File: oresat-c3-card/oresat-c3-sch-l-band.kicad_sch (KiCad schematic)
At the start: 71 parts, among them U15 Qorvo 856930, U16 AT86RF215, U17 SI4112-GM, U2 BP0805A1308, U23 NCS2-62+, U3 BP0805A1308, U4 BGB741L7ESD, U41 TQP3M9036, U5 BP0805A1308, U7 MAC-24+, X1 TXETALSANF-26.000000

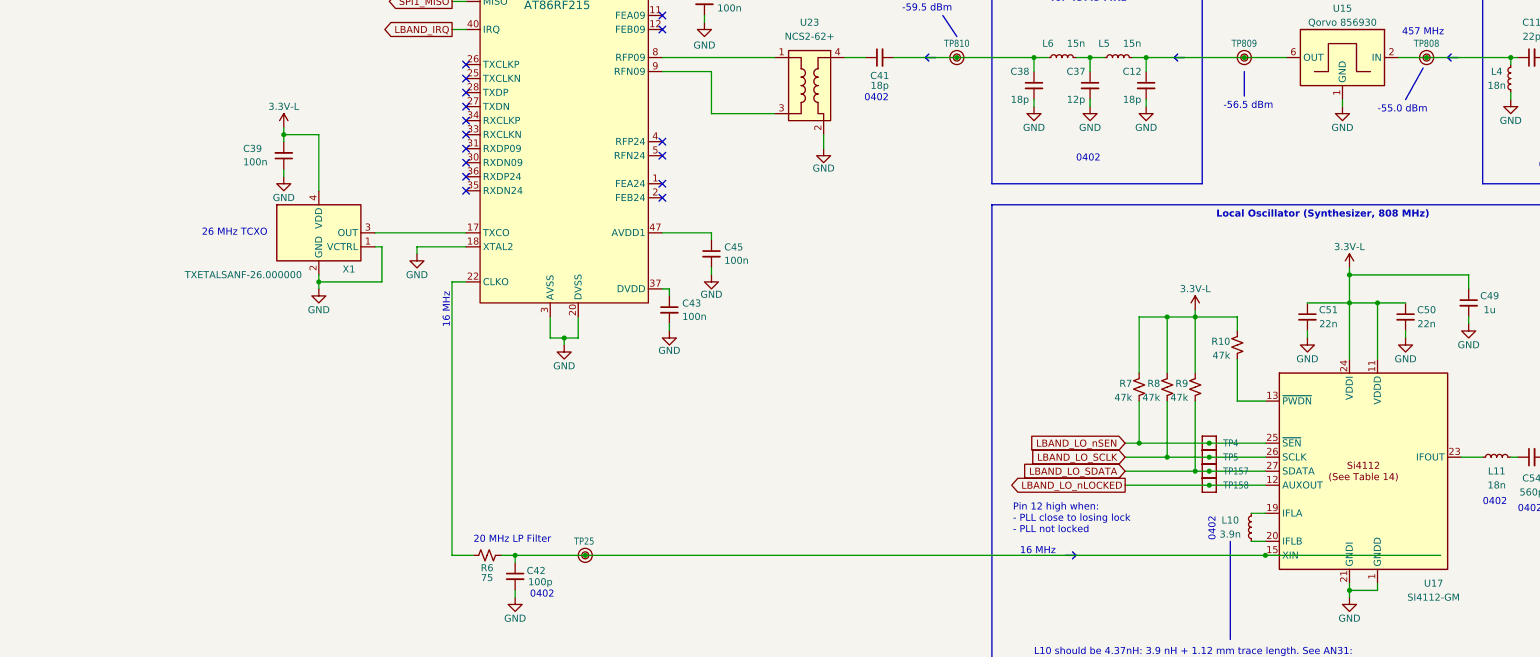
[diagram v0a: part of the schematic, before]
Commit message: Updated footprints to latest KiCad; optimize L band AT86 placement, cleanup UHF AT86 connections
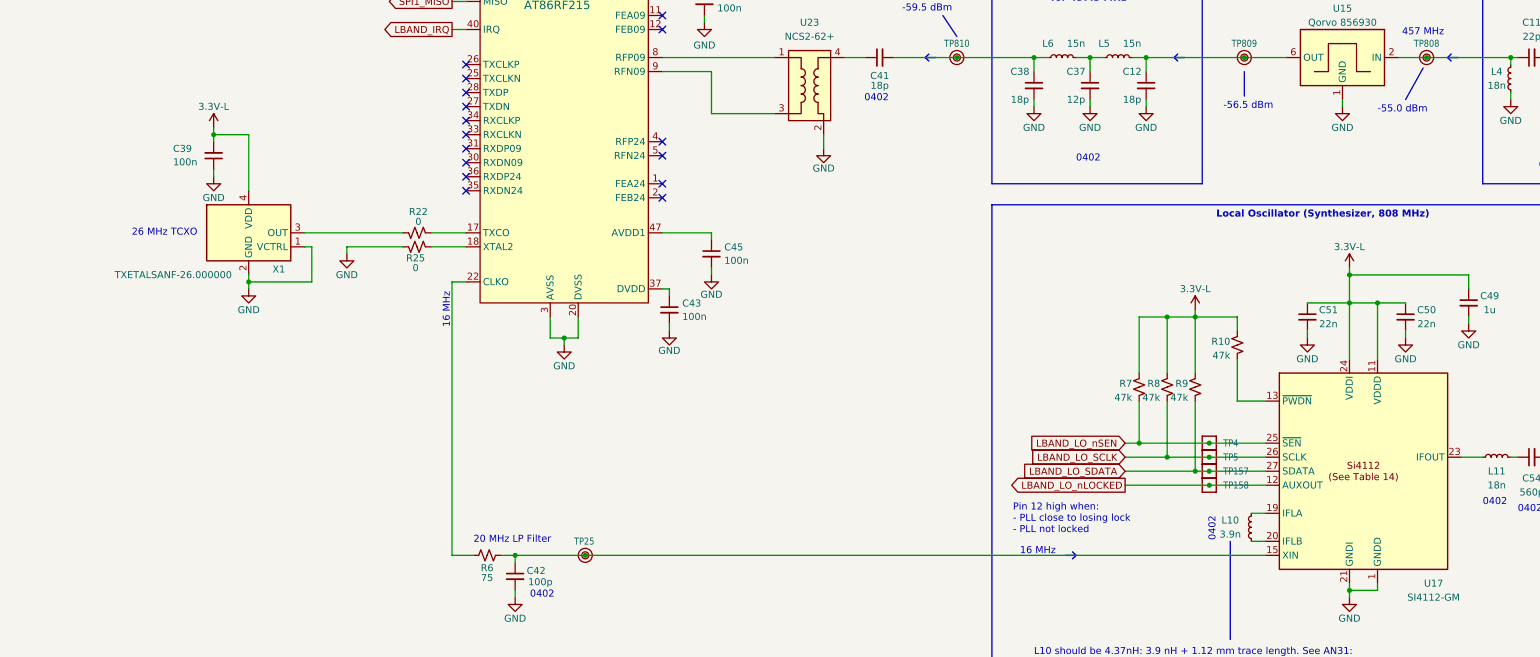
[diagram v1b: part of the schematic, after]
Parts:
- added R22, R25: 0, oresat-passives:0603-C-NOSILK, symbol Device:R_Small_US
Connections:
- net GND: now also R25.2; no longer U16.18 (XTAL2)
- net at U16.17 (TXCO): now also R22.1; no longer X1.3 (OUT)
- new net: R25.1, U16.18 (XTAL2)
- new net: R22.2, X1.3 (OUT)
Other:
- moved on the sheet: C39, X1

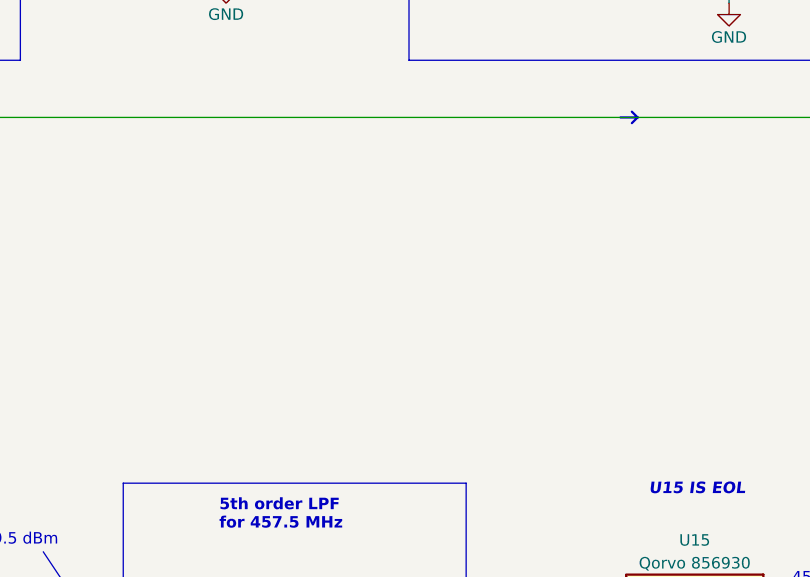
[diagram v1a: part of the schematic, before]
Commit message: L band shield and optimization
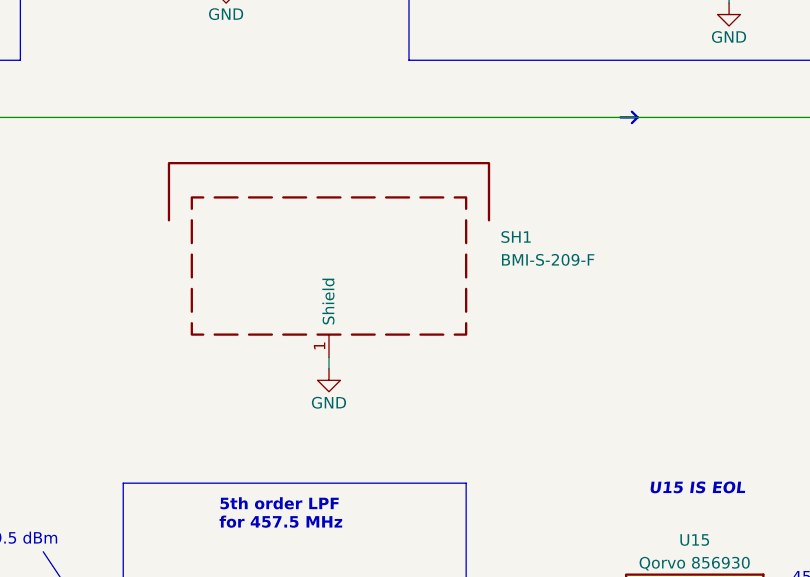
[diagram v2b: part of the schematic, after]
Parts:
- added SH1: BMI-S-209-F, RF_Shielding:Laird_Technologies_BMI-S-209-F_29.36x18.50mm, symbol Device:RFShield_TwoPieces
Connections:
- net GND: now also SH1.1 (Shield)
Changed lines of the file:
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@@
 	(wire
 		(pts
+			(xy 257.81 113.03) (xy 257.81 111.76)
+		)
+		(stroke
+			(width 0)
+			(type default)
+		)
+	)
+	(wire
+		(pts
 			(xy 262.89 143.51) (xy 262.89 140.97)
 		)
@@
 	)
 	(symbol
+		(lib_id "Device:RFShield_TwoPieces")
+		(at 257.81 101.6 0)
+		(unit 1)
+		(exclude_from_sim no)
+		(in_bom yes)
+		(on_board yes)
+		(dnp no)
+		(fields_autoplaced yes)
+		(property "Reference" "SH1"
+			(at 276.86 98.4249 0)
+			(effects
+				(font
+					(size 1.27 1.27)
+				)
+				(justify left)
+			)
+		)
+		(property "Value" "BMI-S-209-F"
+			(at 276.86 100.9649 0)
+			(effects
+				(font
+					(size 1.27 1.27)
+				)
+				(justify left)
+			)
+		)
+		(property "Footprint" "RF_Shielding:Laird_Technologies_BMI-S-209-F_29.36x18.50mm"
+			(at 257.81 104.14 0)
+			(effects
+				(font
+					(size 1.27 1.27)
+				)
+				(hide yes)
+			)
+		)
+		(property "Datasheet" "~"
+			(at 257.81 104.14 0)
+			(effects
+				(font
+					(size 1.27 1.27)
+				)
+				(hide yes)
+			)
+		)
+		(property "Description" "Two-piece EMI RF shielding cabinet"
+			(at 257.81 101.6 0)
+			(effects
+				(font
+					(size 1.27 1.27)
+				)
+				(hide yes)
+			)
+		)
+		(pin "1"
+		)
+		(instances
+			(project ""
+				(path "/65d12cdd-c326-4033-9053-c59fa4e0b25e/1b68ea4b-cacf-4529-b1d4-9be5d7c1043c"
+					(reference "SH1")
+					(unit 1)
+				)
+			)
+		)
+	)
+	(symbol
 		(lib_id "Device:C_Small")
 		(at 73.66 93.98 0)
@@
 					(unit 1)
 				)
+			)
+		)
+	)
+	(symbol
+		(lib_id "power:GND")
+		(at 257.81 113.03 0)
+		(unit 1)
+		(exclude_from_sim no)
+		(in_bom yes)
+		(on_board yes)
+		(dnp no)
+		(property "Reference" "#PWR017"
+			(at 257.81 119.38 0)
+			(effects
+				(font
+					(size 1.27 1.27)
+				)
+				(hide yes)
+			)
+		)
+		(property "Value" "GND"
+			(at 257.81 116.84 0)
+			(effects
+				(font
+					(size 1.27 1.27)
+				)
+			)
+		)
+		(property "Footprint" ""
+			(at 257.81 113.03 0)
+			(effects
+				(font
+					(size 1.27 1.27)
+				)
+				(hide yes)
+			)
+		)
+		(property "Datasheet" ""
+			(at 257.81 113.03 0)
+			(effects
+				(font
+					(size 1.27 1.27)
+				)
+				(hide yes)
+			)
+		)
+		(property "Description" "Power symbol creates a global label with name \"GND\" , ground"
+			(at 257.81 113.03 0)
+			(effects
+				(font
+					(size 1.27 1.27)
+				)
+				(hide yes)
+			)
+		)
+		(pin "1"
+		)
+		(instances
+			(project "oresat-c3"
+				(path "/65d12cdd-c326-4033-9053-c59fa4e0b25e/1b68ea4b-cacf-4529-b1d4-9be5d7c1043c"
+					(reference "#PWR017")
+					(unit 1)
+				)

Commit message: UHF optimized. Ready for polishing
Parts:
- added TP43: ~, oresat-misc:TestPoint_RF_Probe, symbol oresat-misc:Test-Point-RF-Probe-Stripline
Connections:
- net at C41.1, U23.4: now also TP43.1
- net at L11.1, U17.23 (IFOUT): now also TP801.1
- net at C54.2, U7.10 (LO): no longer TP801.1
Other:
- moved on the sheet: C41, C54, L11, TP801
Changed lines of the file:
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@@
 	(text "-2.8 dBm\n"
 		(exclude_from_sim no)
-		(at 363.22 178.435 0)
+		(at 330.454 204.47 0)
 		(effects
 			(font
@@
 	(text "808 MHz"
 		(exclude_from_sim no)
-		(at 356.87 171.45 0)
+		(at 331.724 202.184 0)
 		(effects
 			(font
@@
 	)
 	(junction
+		(at 325.12 213.36)
+		(diameter 0)
+		(color 0 0 0 0)
+	)
+	(junction
 		(at 299.72 180.34)
 		(diameter 0)
@@
 	)
 	(junction
+		(at 212.09 140.97)
+		(diameter 0)
+		(color 0 0 0 0)
+	)
+	(junction
 		(at 231.14 60.96)
 		(diameter 0)
@@
 	)
 	(junction
-		(at 355.6 173.99)
-		(diameter 0)
-		(color 0 0 0 0)
-	)
-	(junction
 		(at 100.33 181.61)
 		(diameter 0)
@@
 	(wire
 		(pts
-			(xy 217.17 140.97) (xy 228.6 140.97)
+			(xy 222.25 140.97) (xy 228.6 140.97)
 		)
 		(stroke
@@
 	(wire
 		(pts
-			(xy 328.93 213.36) (xy 330.2 213.36)
+			(xy 334.01 213.36) (xy 335.28 213.36)
 		)
 		(stroke
@@
 	(wire
 		(pts
+			(xy 212.09 140.97) (xy 217.17 140.97)
+		)
+		(stroke
+			(width 0)
+			(type default)
+		)
+	)
+	(wire
+		(pts
 			(xy 182.88 128.27) (xy 182.88 127)
 		)
@@
 		)
 	)
-	(wire
-		(pts
-			(xy 355.6 173.99) (xy 355.6 151.13)
-		)
-		(stroke
-			(width 0)
-			(type default)
-		)
-	)
 	(polyline
 		(pts
@@
 	(polyline
 		(pts
-			(xy 363.22 176.53) (xy 357.505 173.99)
+			(xy 330.2 205.105) (xy 326.39 209.55)
 		)
 		(stroke
@@
 	(wire
 		(pts
-			(xy 335.28 213.36) (xy 355.6 213.36)
+			(xy 340.36 213.36) (xy 355.6 213.36)
 		)
 		(stroke
@@
 	(wire
 		(pts
-			(xy 320.04 213.36) (xy 323.85 213.36)
+			(xy 320.04 213.36) (xy 325.12 213.36)
 		)
 		(stroke
@@
 	(wire
 		(pts
-			(xy 355.6 213.36) (xy 355.6 173.99)
+			(xy 355.6 151.13) (xy 355.6 213.36)
 		)
 		(stroke
@@
 	(wire
 		(pts
+			(xy 325.12 213.36) (xy 328.93 213.36)
+		)
+		(stroke
+			(width 0)
+			(type default)
+		)
+	)
+	(wire
+		(pts
 			(xy 279.4 203.2) (xy 284.48 203.2)
 		)
@@
 	)
 	(symbol
+		(lib_id "oresat-misc:Test-Point-RF-Probe-Stripline")
+		(at 212.09 140.97 180)
+		(unit 1)
+		(exclude_from_sim no)
+		(in_bom no)
+		(on_board yes)
+		(dnp no)
+		(property "Reference" "TP43"
+			(at 212.09 138.43 0)
+			(effects
+				(font
+					(size 1.27 1.0795)
+				)
+			)
+		)
+		(property "Value" "~"
+			(at 212.09 148.59 0)
+			(effects
+				(font
+					(size 1.27 1.27)
+				)
+				(hide yes)
+			)
+		)
+		(property "Footprint" "oresat-misc:TestPoint_RF_Probe"
+			(at 212.09 151.13 0)
+			(effects
+				(font
+					(size 1.27 1.27)
+				)
+				(hide yes)
+			)
+		)
+		(property "Datasheet" ""
+			(at 212.09 140.97 0)
+			(effects
+				(font
+					(size 1.27 1.27)
+				)
+				(hide yes)
+			)
+		)
+		(property "Description" "Special test point symbol for RF3B-BC2.0 3 needle RFspring probe"
+			(at 212.09 140.97 0)
+			(effects
+				(font
+					(size 1.27 1.27)
+				)
+				(hide yes)
+			)
+		)
+		(pin "1"
+		)
+		(instances
+			(project "oresat-c3"
+				(path "/65d12cdd-c326-4033-9053-c59fa4e0b25e/1b68ea4b-cacf-4529-b1d4-9be5d7c1043c"
+					(reference "TP43")
+					(unit 1)
+				)
+			)
+		)
+	)
+	(symbol
 		(lib_id "Device:L_Small")
 		(at 179.07 55.88 0)
@@
 	(symbol
 		(lib_id "Device:C_Small")
-		(at 214.63 140.97 90)
+		(at 219.71 140.97 90)
 		(mirror x)
 		(unit 1)
@@
 		(dnp no)
 		(property "Reference" "C41"
-			(at 214.63 144.272 90)
+			(at 219.71 144.272 90)
 			(effects
 				(font
@@
 		)
 		(property "Value" "18p"
-			(at 214.63 146.05 90)
+			(at 219.71 146.05 90)
 			(effects
 				(font
@@
 		)
 		(property "Footprint" "Capacitor_SMD:C_0402_1005Metric"
-			(at 214.63 140.97 0)
+			(at 219.71 140.97 0)
 			(effects
 				(font
@@
 		)
 		(property "Datasheet" "~"
-			(at 214.63 140.97 0)
+			(at 219.71 140.97 0)
 			(effects
 				(font
@@
 		)
 		(property "Description" "18pF ±5% 50V Ceramic Capacitor C0G, NP0 0402 (1005 Metric)"
-			(at 214.63 140.97 0)
+			(at 219.71 140.97 0)
 			(effects
 				(font
@@
 		)
 		(property "DPN" "399-15952-1-ND"
-			(at 214.63 140.97 0)
+			(at 219.71 140.97 0)
 			(effects
 				(font
@@
 		)
 		(property "DST" "Digi-Key"
-			(at 214.63 140.97 0)
+			(at 219.71 140.97 0)
 			(effects
 				(font
@@
 		)
 		(property "MFR" "KEMET"
-			(at 214.63 140.97 0)
+			(at 219.71 140.97 0)
 			(effects
 				(font
@@
 		)
 		(property "MPN" "C0402C180J5GACAUTO"
-			(at 214.63 140.97 0)
+			(at 219.71 140.97 0)
 			(effects
 				(font
@@
 	(symbol
 		(lib_id "oresat-misc:Test-Point-RF-Probe-Stripline")
-		(at 355.6 173.99 90)
+		(at 325.12 213.36 0)
 		(unit 1)
 		(exclude_from_sim no)
@@
 		(dnp no)
 		(property "Reference" "TP801"
-			(at 353.06 173.99 0)
+			(at 325.12 210.82 0)
 			(effects
 				(font
@@
 		)
 		(property "Value" "~"
-			(at 347.98 173.99 0)
+			(at 325.12 205.74 0)
 			(effects
 				(font
@@
 		)
 		(property "Footprint" "oresat-misc:TestPoint_RF_Probe"
-			(at 345.44 173.99 0)
+			(at 325.12 203.2 0)
 			(effects
 				(font
@@
 		)
 		(property "Datasheet" ""
-			(at 355.6 173.99 0)
+			(at 325.12 213.36 0)
 			(effects
 				(font
@@
 		)
 		(property "Description" "Special test point symbol for RF3B-BC2.0 3 needle RFspring probe"
-			(at 355.6 173.99 0)
+			(at 325.12 213.36 0)
 			(effects
 				(font
@@
 	(symbol
 		(lib_id "Device:C_Small")
-		(at 332.74 213.36 90)
+		(at 337.82 213.36 90)
 		(unit 1)
 		(exclude_from_sim no)
@@
 		(dnp no)
 		(property "Reference" "C54"
-			(at 332.74 217.17 90)
+			(at 337.82 217.17 90)
 			(effects
 				(font
@@
 		)
 		(property "Value" "560p"
-			(at 332.74 219.71 90)
+			(at 337.82 219.71 90)
 			(effects
 				(font
@@
 		)
 		(property "Footprint" "Capacitor_SMD:C_0402_1005Metric"
-			(at 332.74 213.36 0)
+			(at 337.82 213.36 0)
 			(effects
 				(font
@@
 		)
 		(property "Datasheet" "~"
-			(at 332.74 213.36 0)
+			(at 337.82 213.36 0)
 			(effects
 				(font
@@
 		)
 		(property "Description" "560pF ±5% 50V Ceramic Capacitor C0G, NP0 0402 (1005 Metric)"
-			(at 332.74 213.36 0)
+			(at 337.82 213.36 0)
 			(effects
 				(font
@@
 		)
 		(property "DPN" "399-15868-1-ND"
-			(at 332.74 213.36 0)
+			(at 337.82 213.36 0)
 			(effects
 				(font
@@
 		)
 		(property "DST" "Digi-Key"
-			(at 332.74 213.36 0)
+			(at 337.82 213.36 0)
 			(effects
 				(font
@@
 		)
 		(property "MFR" "KEMET"
-			(at 332.74 213.36 0)
+			(at 337.82 213.36 0)
 			(effects
 				(font
@@
 		)
 		(property "MPN" "C0402C561J5GACAUTO"
-			(at 332.74 213.36 0)
+			(at 337.82 213.36 0)
 			(effects
 				(font
@@
 	(symbol
 		(lib_id "Device:L_Small")
-		(at 326.39 213.36 90)
+		(at 331.47 213.36 90)
 		(unit 1)
 		(exclude_from_sim no)
@@
 		(dnp no)
 		(property "Reference" "L11"
-			(at 326.39 215.9 90)
+			(at 331.47 215.9 90)
 			(effects
 				(font
@@
 		)
 		(property "Value" "18n"
-			(at 326.39 218.44 90)
+			(at 331.47 218.44 90)
 			(effects
 				(font
@@
 		)
 		(property "Footprint" "Inductor_SMD:L_0402_1005Metric"
-			(at 326.39 213.36 0)
+			(at 331.47 213.36 0)
 			(effects
 				(font
@@
 		)
 		(property "Datasheet" "~"
-			(at 326.39 213.36 0)
+			(at 331.47 213.36 0)
 			(effects
 				(font
@@
 		)
 		(property "Description" "18nH Unshielded Wirewound Inductor 900mA 120mOhm 0402 (1005 Metric)"
-			(at 326.39 213.36 0)
+			(at 331.47 213.36 0)
 			(effects
 				(font
@@
 		)
 		(property "DPN" "2035-1083-1-ND"
-			(at 326.39 213.36 0)
+			(at 331.47 213.36 0)
 			(effects
 				(font
@@
 		)
 		(property "DST" "Digi-Key"
-			(at 326.39 213.36 0)
+			(at 331.47 213.36 0)
 			(effects
 				(font
@@
 		)
 		(property "MFR" "Delta Electronics/Components"
-			(at 326.39 213.36 0)
+			(at 331.47 213.36 0)
 			(effects
 				(font
@@
 		)
 		(property "MPN" "0402HP-18NXGL"
-			(at 326.39 213.36 0)
+			(at 331.47 213.36 0)
 			(effects
 				(font
